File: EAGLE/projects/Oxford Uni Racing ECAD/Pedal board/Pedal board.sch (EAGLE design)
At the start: 46 parts, among them IC1 AD711N, J1 ASS + BOTS, J2 THR_1_2, J3 PWR_CAN, J6 BR_POS_PRESS_STWH, J7 T821108A1S100CEU, K2 EC2-12TNU, T1 BT169, X2 D-SUB9-H2M09ST

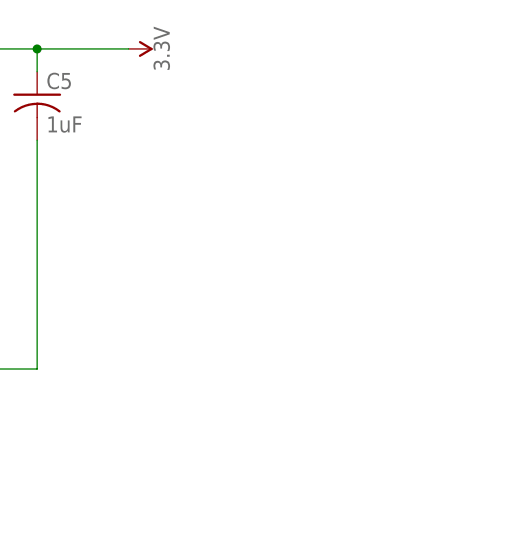
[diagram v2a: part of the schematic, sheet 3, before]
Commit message: added indicator LEDs to boards
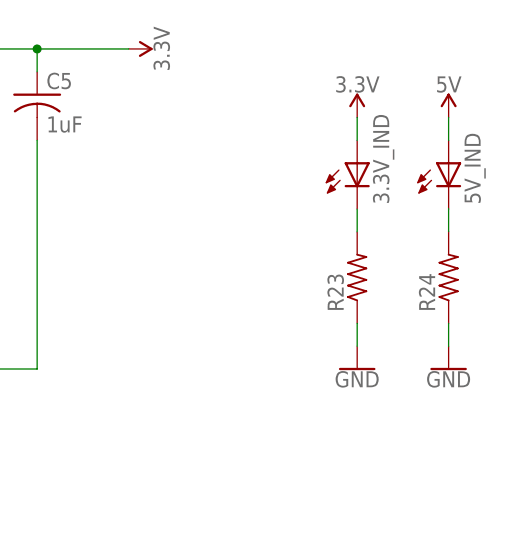
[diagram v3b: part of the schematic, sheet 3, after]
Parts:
- added 3.3V_IND, 5V_IND: (no value), adafruit:LED3MM
- added R23, R24: (no value), adafruit:R-US_0204/7
- BRAKE_LIGHTS: value 2A -> 1A
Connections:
- new net N$12: 3.3V_IND.C, R23.2
- new net N$4: 5V_IND.C, R24.2
- net 3.3V: now also 3.3V_IND.A
- net 5V: now also 5V_IND.A
- net GND: now also R23.1, R24.1
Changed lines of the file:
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@@
 <part name="SUPPLY1" library="SparkFun-PowerSymbols" library_urn="urn:adsk.eagle:library:530" deviceset="5V" device=""/>
 <part name="F1" library="fuse" library_urn="urn:adsk.eagle:library:233" deviceset="FUSE" device="BLANK_5X20MM" package3d_urn="urn:adsk.eagle:package:14079/1" value="1A"/>
-<part name="BRAKE_LIGHTS" library="fuse" library_urn="urn:adsk.eagle:library:233" deviceset="FUSE" device="BLANK_5X20MM" package3d_urn="urn:adsk.eagle:package:14079/1" value="2A"/>
+<part name="BRAKE_LIGHTS" library="fuse" library_urn="urn:adsk.eagle:library:233" deviceset="FUSE" device="BLANK_5X20MM" package3d_urn="urn:adsk.eagle:package:14079/1" value="1A"/>
 <part name="R1" library="adafruit" library_urn="urn:adsk.eagle:library:420" deviceset="R-US_" device="0204/7" package3d_urn="urn:adsk.eagle:package:6240596/1" value="1M"/>
 <part name="R2" library="adafruit" library_urn="urn:adsk.eagle:library:420" deviceset="R-US_" device="0204/7" package3d_urn="urn:adsk.eagle:package:6240596/1" value="1M"/>
@@
 <part name="SUPPLY44" library="SparkFun-PowerSymbols" library_urn="urn:adsk.eagle:library:530" deviceset="5V" device=""/>
 <part name="SUPPLY45" library="SparkFun-PowerSymbols" library_urn="urn:adsk.eagle:library:530" deviceset="5V" device=""/>
+<part name="3.3V_IND" library="adafruit" library_urn="urn:adsk.eagle:library:420" deviceset="LED" device="3MM" package3d_urn="urn:adsk.eagle:package:6240537/1"/>
+<part name="R23" library="adafruit" library_urn="urn:adsk.eagle:library:420" deviceset="R-US_" device="0204/7" package3d_urn="urn:adsk.eagle:package:6240596/1"/>
+<part name="SUPPLY47" library="SparkFun-PowerSymbols" library_urn="urn:adsk.eagle:library:530" deviceset="3.3V" device=""/>
+<part name="GND30" library="SparkFun-PowerSymbols" library_urn="urn:adsk.eagle:library:530" deviceset="GND" device=""/>
+<part name="5V_IND" library="adafruit" library_urn="urn:adsk.eagle:library:420" deviceset="LED" device="3MM" package3d_urn="urn:adsk.eagle:package:6240537/1"/>
+<part name="R24" library="adafruit" library_urn="urn:adsk.eagle:library:420" deviceset="R-US_" device="0204/7" package3d_urn="urn:adsk.eagle:package:6240596/1"/>
+<part name="SUPPLY54" library="SparkFun-PowerSymbols" library_urn="urn:adsk.eagle:library:530" deviceset="5V" device=""/>
+<part name="GND33" library="SparkFun-PowerSymbols" library_urn="urn:adsk.eagle:library:530" deviceset="GND" device=""/>
 </parts>
 <sheets>
@@
 <attribute name="VALUE" x="155.194" y="119.38" size="1.778" layer="96" rot="R270" align="bottom-center"/>
 </instance>
+<instance part="3.3V_IND" gate="G$1" x="177.8" y="106.68" smashed="yes">
+<attribute name="NAME" x="181.356" y="102.108" size="1.778" layer="95" rot="R90"/>
+<attribute name="VALUE" x="183.515" y="102.108" size="1.778" layer="96" rot="R90"/>
+</instance>
+<instance part="R23" gate="G$1" x="177.8" y="93.98" smashed="yes" rot="R90">
+<attribute name="NAME" x="176.3014" y="90.17" size="1.778" layer="95" rot="R90"/>
+<attribute name="VALUE" x="181.102" y="90.17" size="1.778" layer="96" rot="R90"/>
+</instance>
+<instance part="SUPPLY47" gate="G$1" x="177.8" y="111.76" smashed="yes">
+<attribute name="VALUE" x="177.8" y="114.554" size="1.778" layer="96" align="bottom-center"/>
+</instance>
+<instance part="GND30" gate="1" x="177.8" y="83.82" smashed="yes">
+<attribute name="VALUE" x="177.8" y="83.566" size="1.778" layer="96" align="top-center"/>
+</instance>
+<instance part="5V_IND" gate="G$1" x="187.96" y="106.68" smashed="yes">
+<attribute name="NAME" x="191.516" y="102.108" size="1.778" layer="95" rot="R90"/>
+<attribute name="VALUE" x="193.675" y="102.108" size="1.778" layer="96" rot="R90"/>
+</instance>
+<instance part="R24" gate="G$1" x="187.96" y="93.98" smashed="yes" rot="R90">
+<attribute name="NAME" x="186.4614" y="90.17" size="1.778" layer="95" rot="R90"/>
+<attribute name="VALUE" x="191.262" y="90.17" size="1.778" layer="96" rot="R90"/>
+</instance>
+<instance part="SUPPLY54" gate="G$1" x="187.96" y="111.76" smashed="yes">
+<attribute name="VALUE" x="187.96" y="114.554" size="1.778" layer="96" align="bottom-center"/>
+</instance>
+<instance part="GND33" gate="1" x="187.96" y="83.82" smashed="yes">
+<attribute name="VALUE" x="187.96" y="83.566" size="1.778" layer="96" align="top-center"/>
+</instance>
 </instances>
 <busses>
@@
 <junction x="132.08" y="60.96"/>
 </segment>
+<segment>
+<pinref part="5V_IND" gate="G$1" pin="A"/>
+<pinref part="SUPPLY54" gate="G$1" pin="5V"/>
+<wire x1="187.96" y1="109.22" x2="187.96" y2="111.76" width="0.1524" layer="91"/>
+</segment>
 </net>
 <net name="3.3V" class="0">
@@
 <pinref part="SUPPLY14" gate="G$1" pin="3.3V"/>
 </segment>
+<segment>
+<pinref part="3.3V_IND" gate="G$1" pin="A"/>
+<pinref part="SUPPLY47" gate="G$1" pin="3.3V"/>
+<wire x1="177.8" y1="109.22" x2="177.8" y2="111.76" width="0.1524" layer="91"/>
+</segment>
 </net>
 <net name="GND" class="0">
@@
 <wire x1="142.24" y1="25.4" x2="121.92" y2="25.4" width="0.1524" layer="91"/>
 </segment>
+<segment>
+<pinref part="R24" gate="G$1" pin="1"/>
+<pinref part="GND33" gate="1" pin="GND"/>
+<wire x1="187.96" y1="88.9" x2="187.96" y2="86.36" width="0.1524" layer="91"/>
+</segment>
+<segment>
+<pinref part="GND30" gate="1" pin="GND"/>
+<pinref part="R23" gate="G$1" pin="1"/>
+<wire x1="177.8" y1="86.36" x2="177.8" y2="88.9" width="0.1524" layer="91"/>
+</segment>
 </net>
 <net name="CANH" class="0">
@@
 </segment>
 </net>
+<net name="N$4" class="0">
+<segment>
+<pinref part="5V_IND" gate="G$1" pin="C"/>
+<pinref part="R24" gate="G$1" pin="2"/>
+<wire x1="187.96" y1="101.6" x2="187.96" y2="99.06" width="0.1524" layer="91"/>
+</segment>
+</net>
+<net name="N$12" class="0">
+<segment>
+<pinref part="R23" gate="G$1" pin="2"/>
+<pinref part="3.3V_IND" gate="G$1" pin="C"/>
+<wire x1="177.8" y1="99.06" x2="177.8" y2="101.6" width="0.1524" layer="91"/>
+</segment>
+</net>

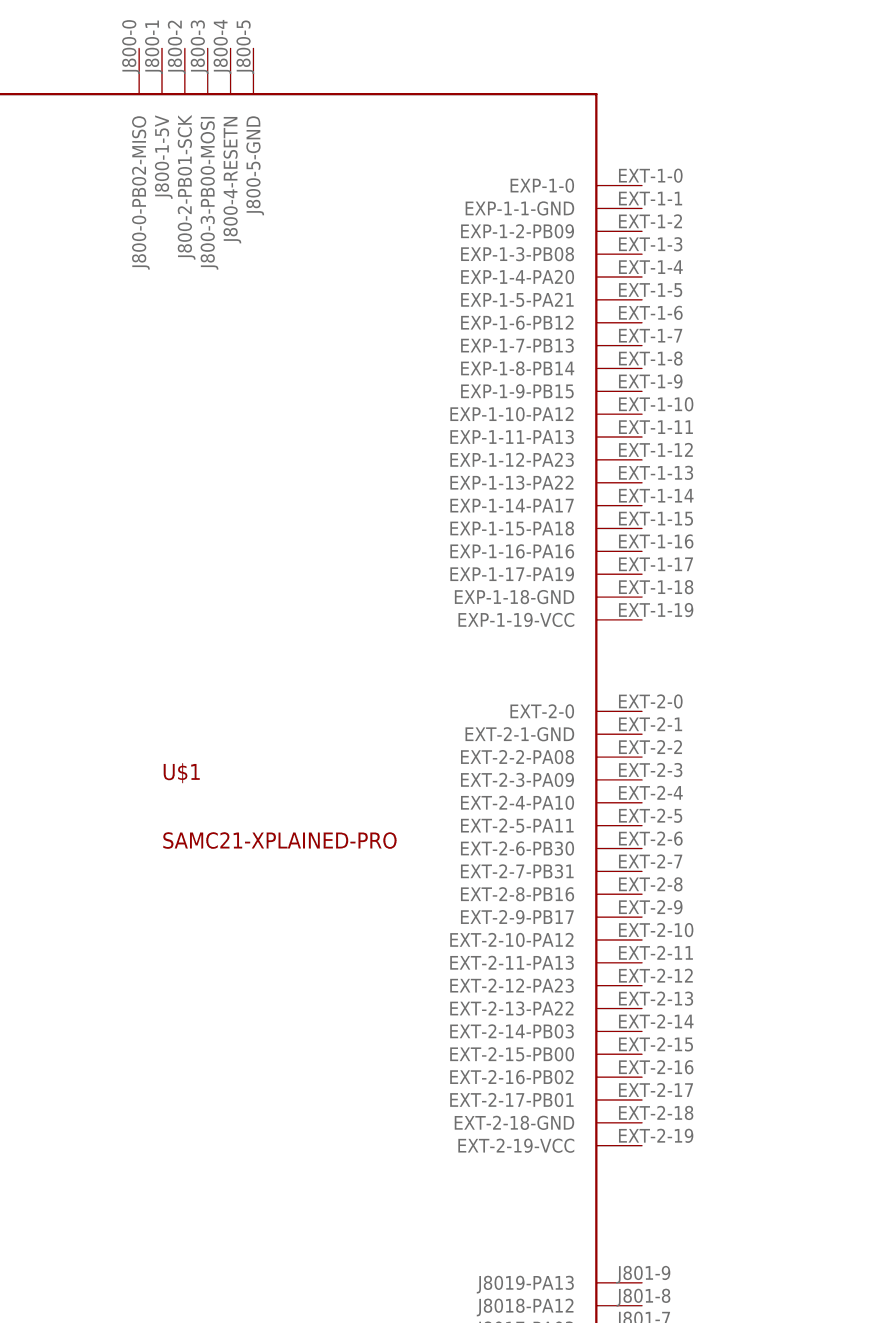
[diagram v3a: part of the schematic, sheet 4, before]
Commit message: replaced MCUs on pedal and dashboard to not include ext1&2
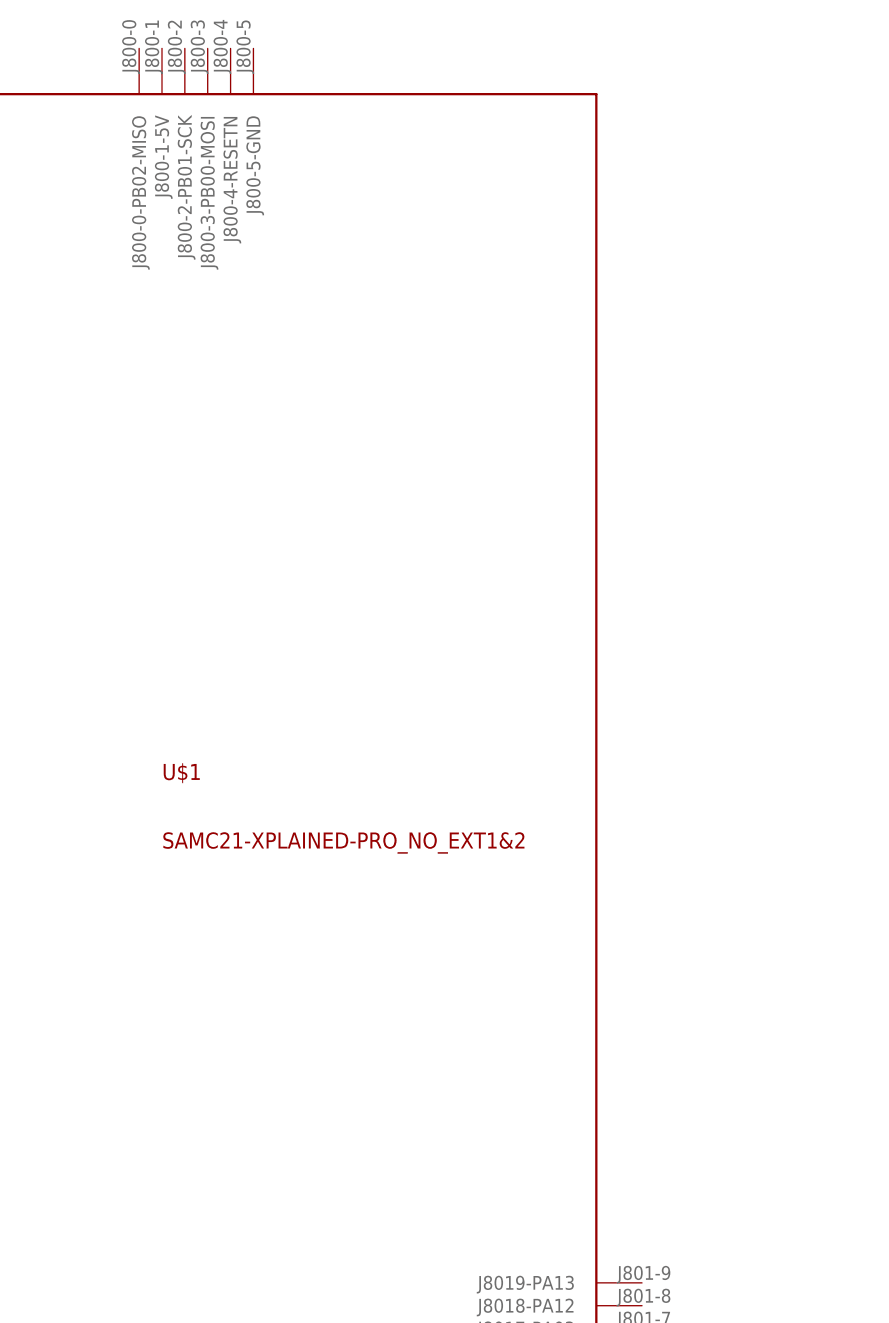
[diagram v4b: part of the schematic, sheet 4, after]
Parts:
- U$1: value SAMC21-XPLAINED-PRO -> SAMC21-XPLAINED-PRO_NO_EXT1&2; device Oxford Uni Racing Custom Blueprints:SAMC21-XPLAINED-PRO -> Oxford Uni Racing Custom Blueprints:SAMC21-XPLAINED-PRO_NO_EXT1&2
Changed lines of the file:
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@@
 <part name="GND12" library="SparkFun-PowerSymbols" library_urn="urn:adsk.eagle:library:530" deviceset="GND" device=""/>
 <part name="GND13" library="SparkFun-PowerSymbols" library_urn="urn:adsk.eagle:library:530" deviceset="GND" device=""/>
-<part name="U$1" library="Oxford Uni Racing Custom Blueprints" deviceset="SAMC21-XPLAINED-PRO" device=""/>
 <part name="SUPPLY23" library="SparkFun-PowerSymbols" library_urn="urn:adsk.eagle:library:530" deviceset="5V" device=""/>
 <part name="GND14" library="SparkFun-PowerSymbols" library_urn="urn:adsk.eagle:library:530" deviceset="GND" device=""/>
@@
 <part name="SUPPLY54" library="SparkFun-PowerSymbols" library_urn="urn:adsk.eagle:library:530" deviceset="5V" device=""/>
 <part name="GND33" library="SparkFun-PowerSymbols" library_urn="urn:adsk.eagle:library:530" deviceset="GND" device=""/>
+<part name="U$1" library="Oxford Uni Racing Custom Blueprints" deviceset="SAMC21-XPLAINED-PRO_NO_EXT1&amp;2" device=""/>
 </parts>
 <sheets>
@@
 <attribute name="VALUE" x="40.894" y="76.2" size="1.778" layer="96" rot="R90" align="top-center"/>
 </instance>
+<instance part="SUPPLY23" gate="G$1" x="162.56" y="33.02" smashed="yes" rot="R90">
+<attribute name="VALUE" x="159.766" y="33.02" size="1.778" layer="96" rot="R90" align="bottom-center"/>
+</instance>
+<instance part="GND14" gate="1" x="154.94" y="27.94" smashed="yes" rot="R270">
+<attribute name="VALUE" x="154.686" y="27.94" size="1.778" layer="96" rot="R270" align="top-center"/>
+</instance>
 <instance part="U$1" gate="G$1" x="180.34" y="-7.62" smashed="yes">
 <attribute name="NAME" x="218.44" y="109.22" size="1.778" layer="94"/>
 <attribute name="VALUE" x="218.44" y="101.6" size="1.778" layer="94"/>
-</instance>
-<instance part="SUPPLY23" gate="G$1" x="162.56" y="33.02" smashed="yes" rot="R90">
-<attribute name="VALUE" x="159.766" y="33.02" size="1.778" layer="96" rot="R90" align="bottom-center"/>
-</instance>
-<instance part="GND14" gate="1" x="154.94" y="27.94" smashed="yes" rot="R270">
-<attribute name="VALUE" x="154.686" y="27.94" size="1.778" layer="96" rot="R270" align="top-center"/>
 </instance>
 </instances>
@@
 </segment>
 <segment>
-<pinref part="U$1" gate="G$1" pin="J802-4-5V"/>
 <wire x1="175.26" y1="33.02" x2="162.56" y2="33.02" width="0.1524" layer="91"/>
 <pinref part="SUPPLY23" gate="G$1" pin="5V"/>
+<pinref part="U$1" gate="G$1" pin="J802-4-5V"/>
 </segment>
 </net>
@@
 </segment>
 <segment>
-<pinref part="U$1" gate="G$1" pin="J802-5-GND"/>
 <wire x1="175.26" y1="30.48" x2="162.56" y2="30.48" width="0.1524" layer="91"/>
-<pinref part="U$1" gate="G$1" pin="J802-6GND"/>
 <wire x1="175.26" y1="27.94" x2="162.56" y2="27.94" width="0.1524" layer="91"/>
 <wire x1="162.56" y1="30.48" x2="162.56" y2="27.94" width="0.1524" layer="91"/>
@@
 <wire x1="162.56" y1="27.94" x2="157.48" y2="27.94" width="0.1524" layer="91"/>
 <junction x="162.56" y="27.94"/>
+<pinref part="U$1" gate="G$1" pin="J802-5-GND"/>
+<pinref part="U$1" gate="G$1" pin="J802-6GND"/>
 </segment>
 </net>
@@
 </segment>
 <segment>
-<pinref part="U$1" gate="G$1" pin="CAN0-CANH"/>
 <wire x1="175.26" y1="58.42" x2="162.56" y2="58.42" width="0.1524" layer="91"/>
 <label x="157.48" y="58.42" size="1.778" layer="95"/>
+<pinref part="U$1" gate="G$1" pin="CAN0-CANH"/>
 </segment>
 </net>
@@
 </segment>
 <segment>
-<pinref part="U$1" gate="G$1" pin="CAN1-CANL"/>
 <wire x1="175.26" y1="60.96" x2="162.56" y2="60.96" width="0.1524" layer="91"/>
 <label x="157.48" y="60.96" size="1.778" layer="95"/>
+<pinref part="U$1" gate="G$1" pin="CAN1-CANL"/>
 </segment>
 </net>
@@
 </segment>
 <segment>
-<pinref part="U$1" gate="G$1" pin="J803-0-PB09"/>
 <wire x1="175.26" y1="17.78" x2="162.56" y2="17.78" width="0.1524" layer="91"/>
 <label x="147.32" y="17.78" size="1.778" layer="95"/>
+<pinref part="U$1" gate="G$1" pin="J803-0-PB09"/>
 </segment>
 </net>
@@
 </segment>
 <segment>
-<pinref part="U$1" gate="G$1" pin="J803-1-PB08"/>
 <wire x1="175.26" y1="15.24" x2="162.56" y2="15.24" width="0.1524" layer="91"/>
 <label x="147.32" y="15.24" size="1.778" layer="95"/>
+<pinref part="U$1" gate="G$1" pin="J803-1-PB08"/>
 </segment>
 </net>
@@
 </segment>
 <segment>
-<pinref part="U$1" gate="G$1" pin="J803-2-PA08"/>
 <wire x1="175.26" y1="12.7" x2="162.56" y2="12.7" width="0.1524" layer="91"/>
 <label x="147.32" y="12.7" size="1.778" layer="95"/>
+<pinref part="U$1" gate="G$1" pin="J803-2-PA08"/>
 </segment>
 </net>
@@
 </segment>
 <segment>
-<pinref part="U$1" gate="G$1" pin="J803-4-PB07"/>
 <wire x1="175.26" y1="7.62" x2="162.56" y2="7.62" width="0.1524" layer="91"/>
 <label x="147.32" y="7.62" size="1.778" layer="95"/>
+<pinref part="U$1" gate="G$1" pin="J803-4-PB07"/>
 </segment>
 </net>
@@
 </segment>
 <segment>
-<pinref part="U$1" gate="G$1" pin="J804-2-PA20"/>
 <wire x1="271.78" y1="7.62" x2="289.56" y2="7.62" width="0.1524" layer="91"/>
 <label x="289.56" y="7.62" size="1.778" layer="95"/>
+<pinref part="U$1" gate="G$1" pin="J804-2-PA20"/>
 </segment>
 </net>
@@
 </segment>
 <segment>
-<pinref part="U$1" gate="G$1" pin="J803-5-PB06"/>
 <wire x1="175.26" y1="5.08" x2="162.56" y2="5.08" width="0.1524" layer="91"/>
 <label x="147.32" y="5.08" size="1.778" layer="95"/>
+<pinref part="U$1" gate="G$1" pin="J803-5-PB06"/>
 </segment>
 </net>
@@
 </segment>
 <segment>
-<pinref part="U$1" gate="G$1" pin="J803-3-PA09"/>
 <wire x1="175.26" y1="10.16" x2="162.56" y2="10.16" width="0.1524" layer="91"/>
 <label x="147.32" y="10.16" size="1.778" layer="95"/>
-</segment>
-</net>
+<pinref part="U$1" gate="G$1" pin="J803-3-PA09"/>
+</segment>
+</net>

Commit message: removed brake lights from pedal board
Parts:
- removed BRAKE_LIGHTS: 1A, fuse:FUSEBLANK_5X20MM
- removed BR_LIGHTS_TR: IRLML2502GTRPBF, adafruit:MOSFET-NREFLOW
- removed J7: T821108A1S100CEU, T821108A1S100CEU:T821108A1S100CEU
- removed R12: 1K, adafruit:R-US_0204/7
- removed R13: 47K, adafruit:R-US_0204/7
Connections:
- removed net 12V_BR_LIGHTS: BRAKE_LIGHTS.2, J7.8
- removed net BRAKE_LIGHTS_OUT: R12.1, U$1.J804-2-PA20
- removed net N$25: BR_LIGHTS_TR.G, R12.2, R13.2
- removed net N$28: BR_LIGHTS_TR.D, J7.3
- net 12V_BATTERY: no longer BRAKE_LIGHTS.1
- net BR_POSS2: no longer U$1.J803-3-PA09
- net GND: no longer BR_LIGHTS_TR.S, R13.1
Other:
- note removed: "BRAKE LIGHTS CONNECTOR"
